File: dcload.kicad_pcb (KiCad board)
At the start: 2 copper layers, 251.4 x 94.7 mm, 12 parts

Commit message: General dimension tweaks
 - My understanding of exterior routing was incorrect resulting in
   unusable exterior dimensions.
 - Reduced tolerancing on D punches for tighter fit
 - Dropped LCD down slightly so not as close to edge
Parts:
- moved REF** 1.00 mm to (82.2, 48.8)
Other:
- board size 251.4 x 94.7 mm -> 249.8 x 93.1 mm
- board text added: "Exterior Dimensions: 249.81mm x 93.14mm"
- board text added: "July 7, 2018 V2 Phelps Williams"
- board text removed: "July 1, 2018 V1 Phelps Williams"
- board text removed: "Notes: - Exterior Routing with 1.6mm bit - Interior Nonplated Slots with 0.8mm bit - Exterior Dimensions: 249.81mm x 93.14mm"
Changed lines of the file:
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@@
     (links 0)
     (no_connects 0)
-    (area 13.099999 -113.850001 590.350001 126.71)
+    (area 15.024999 16.524999 264.985001 124.16)
     (thickness 1.6)
     (drawings 31)
@@
     (pad_to_mask_clearance 0.2)
     (aux_axis_origin 0 0)
-    (visible_elements FFFFFF7F)
+    (visible_elements FFFFFF6F)
     (pcbplotparams
       (layerselection 0x012f0_80000001)
@@
       (psa4output false)
       (plotreference true)
-      (plotvalue true)
+      (plotvalue false)
       (plotinvisibletext false)
       (padsonsilk false)
@@
       (drillshape 0)
       (scaleselection 1)
-      (outputdirectory ""))
+      (outputdirectory gerbers/))
   )
   (net 0 "")
@@
     (uvia_drill 0.1)
   )
-  (module p_panel_holes:Keystone_4093_DualBindingPost (layer F.Cu)
-    (at 120 94.25)
-    (fp_text reference REF** (at 0 -7.35) (layer F.SilkS) hide
-      (effects (font (size 1 1) (thickness 0.15)))
-    )
-    (fp_text value Keystone_4093_DualBindingPost (at 0 7.8) (layer F.Fab) hide
-      (effects (font (size 1 1) (thickness 0.15)))
-    )
-    (fp_line (start -15.225 -3.1) (end -15.225 3.1) (layer Edge.Cuts) (width 0.8))
-    (fp_arc (start -9.525 0) (end -15.225 -3.1) (angle 301.5) (layer Edge.Cuts) (width 0.8))
-    (fp_arc (start 9.525 0) (end 3.825 -3.1) (angle 301.5) (layer Edge.Cuts) (width 0.8))
-    (fp_line (start 3.825 -3.1) (end 3.825 3.1) (layer Edge.Cuts) (width 0.8))
-  )
   (module p_panel_holes:100DP1T1B1M1QEH (layer F.Cu)
     (at 90 94.25 180)
@@
   )
   (module p_panel_holes:LCD_Panel (layer F.Cu)
-    (at 82.25 47.75)
+    (at 82.25 48.75)
     (fp_text reference REF** (at 0 0.5) (layer F.SilkS)
       (effects (font (size 1 1) (thickness 0.15)))
@@
     (fp_line (start 49.1 30) (end -49.1 30) (layer B.SilkS) (width 0.15))
     (fp_line (start -49.1 30) (end -49.1 -30) (layer B.SilkS) (width 0.15))
-    (fp_line (start -48.9 -20.1) (end 48.9 -20.1) (layer Edge.Cuts) (width 0.8))
-    (fp_line (start 48.9 -20.1) (end 48.9 20.1) (layer Edge.Cuts) (width 0.8))
-    (fp_line (start 48.9 20.1) (end -48.9 20.1) (layer Edge.Cuts) (width 0.8))
-    (fp_line (start -48.9 20.1) (end -48.9 -20.1) (layer Edge.Cuts) (width 0.8))
+    (fp_line (start -48.9 -20.1) (end 48.9 -20.1) (layer Edge.Cuts) (width 0.15))
+    (fp_line (start 48.9 -20.1) (end 48.9 20.1) (layer Edge.Cuts) (width 0.15))
+    (fp_line (start 48.9 20.1) (end -48.9 20.1) (layer Edge.Cuts) (width 0.15))
+    (fp_line (start -48.9 20.1) (end -48.9 -20.1) (layer Edge.Cuts) (width 0.15))
     (pad "" np_thru_hole circle (at -46.5 27.5) (size 3.5 3.5) (drill 3.5) (layers *.Cu *.Mask))
     (pad "" np_thru_hole circle (at -46.5 -27.5) (size 3.5 3.5) (drill 3.5) (layers *.Cu *.Mask))
@@
       (effects (font (size 1 1) (thickness 0.15)))
     )
-    (fp_line (start -15.225 -3.1) (end -15.225 3.1) (layer Edge.Cuts) (width 0.8))
-    (fp_arc (start -9.525 0) (end -15.225 -3.1) (angle 301.5) (layer Edge.Cuts) (width 0.8))
-    (fp_arc (start 9.525 0) (end 3.825 -3.1) (angle 301.5) (layer Edge.Cuts) (width 0.8))
-    (fp_line (start 3.825 -3.1) (end 3.825 3.1) (layer Edge.Cuts) (width 0.8))
-  )
-  (module p_panel_holes:VB1094-75 (layer F.Cu)
-    (at 245.75 63)
-    (fp_text reference REF** (at 0 6.05) (layer F.SilkS) hide
-      (effects (font (size 1 1) (thickness 0.15)))
-    )
-    (fp_text value VB1094-75 (at 0.05 -5.85) (layer F.Fab) hide
-      (effects (font (size 1 1) (thickness 0.15)))
-    )
-    (fp_arc (start 0 0) (end -4.25 -2.67) (angle 295.5) (layer Edge.Cuts) (width 0.8))
-    (fp_line (start -4.25 -2.65) (end -4.25 2.65) (layer Edge.Cuts) (width 0.8))
-    (fp_circle (center 0 0) (end 1.5 0) (layer B.SilkS) (width 0.15))
+    (fp_line (start -15.065 -3.11) (end -15.065 3.11) (layer Edge.Cuts) (width 0.15))
+    (fp_arc (start -9.525 0) (end -15.065 -3.11) (angle 301.3) (layer Edge.Cuts) (width 0.15))
+    (fp_arc (start 9.525 0) (end 3.985 -3.11) (angle 301.3) (layer Edge.Cuts) (width 0.15))
+    (fp_line (start 3.985 -3.11) (end 3.985 3.11) (layer Edge.Cuts) (width 0.15))
+  )
+  (module p_panel_holes:Keystone_4093_DualBindingPost (layer F.Cu)
+    (at 120 94.25)
+    (fp_text reference REF** (at 0 -7.35) (layer F.SilkS) hide
+      (effects (font (size 1 1) (thickness 0.15)))
+    )
+    (fp_text value Keystone_4093_DualBindingPost (at 0 7.8) (layer F.Fab) hide
+      (effects (font (size 1 1) (thickness 0.15)))
+    )
+    (fp_line (start -15.065 -3.11) (end -15.065 3.11) (layer Edge.Cuts) (width 0.15))
+    (fp_arc (start -9.525 0) (end -15.065 -3.11) (angle 301.3) (layer Edge.Cuts) (width 0.15))
+    (fp_arc (start 9.525 0) (end 3.985 -3.11) (angle 301.3) (layer Edge.Cuts) (width 0.15))
+    (fp_line (start 3.985 -3.11) (end 3.985 3.11) (layer Edge.Cuts) (width 0.15))
   )
   (module p_panel_holes:5x4_Matrix_Keypad (layer F.Cu)
@@
     (fp_line (start -1 36.5) (end 1 36.5) (layer F.SilkS) (width 0.15))
     (fp_line (start -42.55 -1) (end -42.55 1) (layer F.SilkS) (width 0.15))
-    (fp_line (start -39.55 -35) (end -13.05 -35) (layer Edge.Cuts) (width 0.8))
-    (fp_line (start -13.05 -35) (end -13.05 -31.5) (layer Edge.Cuts) (width 0.8))
-    (fp_line (start -13.05 -31.5) (end -39.55 -31.5) (layer Edge.Cuts) (width 0.8))
-    (fp_line (start -39.55 -31.5) (end -39.55 -35) (layer Edge.Cuts) (width 0.8))
+    (fp_line (start -39.05 -35) (end -13.55 -35) (layer Edge.Cuts) (width 0.15))
+    (fp_line (start -13.55 -35) (end -13.55 -31.5) (layer Edge.Cuts) (width 0.15))
+    (fp_line (start -13.55 -31.5) (end -39.05 -31.5) (layer Edge.Cuts) (width 0.15))
+    (fp_line (start -39.05 -31.5) (end -39.05 -35) (layer Edge.Cuts) (width 0.15))
     (fp_line (start -42.55 36.5) (end -42.55 -36.5) (layer B.SilkS) (width 0.15))
     (fp_line (start -42.55 -36.5) (end 42.55 -36.5) (layer B.SilkS) (width 0.15))
@@
     (fp_line (start 42.55 36.5) (end -42.55 36.5) (layer B.SilkS) (width 0.15))
   )
-  (gr_text "July 1, 2018\nV1\nPhelps Williams" (at 191.75 57) (layer B.SilkS)
+  (module p_panel_holes:VB1094-75 (layer F.Cu)
+    (at 245.75 63)
+    (fp_text reference REF** (at 0 6.05) (layer F.SilkS) hide
+      (effects (font (size 1 1) (thickness 0.15)))
+    )
+    (fp_text value VB1094-75 (at 0.05 -6.05) (layer F.Fab) hide
+      (effects (font (size 1 1) (thickness 0.15)))
+    )
+    (fp_arc (start 0 0) (end -4.05 -2.67) (angle 293) (layer Edge.Cuts) (width 0.15))
+    (fp_line (start -4.05 -2.67) (end -4.05 2.67) (layer Edge.Cuts) (width 0.15))
+    (fp_circle (center 0 0) (end 1.5 0) (layer B.SilkS) (width 0.15))
+  )
+  (gr_text "July 7, 2018\nV2\nPhelps Williams" (at 191.75 57) (layer B.SilkS)
     (effects (font (size 1.5 1.5) (thickness 0.3)) (justify left mirror))
   )
@@
     (effects (font (size 2 2) (thickness 0.45)))
   )
-  (gr_text "DC Electronic Load" (at 82.25 22.5) (layer F.SilkS)
+  (gr_text "DC Electronic Load" (at 82.25 23) (layer F.SilkS)
     (effects (font (size 3 3) (thickness 0.6)))
   )
@@
   (gr_line (start 255.255 44.08) (end 255.255 82.26) (angle 90) (layer Eco1.User) (width 0.15))
   (gr_line (start 24.755 82.26) (end 24.755 44.08) (angle 90) (layer Eco1.User) (width 0.15))
-  (gr_arc (start 259.37 22.14) (end 259.37 15.8) (angle 90) (layer Edge.Cuts) (width 1.6))
-  (gr_arc (start 259.37 104.2) (end 265.71 104.2) (angle 90) (layer Edge.Cuts) (width 1.6))
-  (gr_arc (start 20.64 104.2) (end 20.64 110.54) (angle 90) (layer Edge.Cuts) (width 1.6))
-  (gr_text "Notes:\n - Exterior Routing with 1.6mm bit\n - Interior Nonplated Slots with 0.8mm bit\n - Exterior Dimensions: 249.81mm x 93.14mm" (at 119.14 122.81) (layer Cmts.User)
+  (gr_arc (start 259.37 22.14) (end 259.37 16.6) (angle 90) (layer Edge.Cuts) (width 0.15))
+  (gr_arc (start 259.37 104.2) (end 264.91 104.2) (angle 90) (layer Edge.Cuts) (width 0.15))
+  (gr_arc (start 20.64 104.2) (end 20.64 109.74) (angle 90) (layer Edge.Cuts) (width 0.15))
+  (gr_text "Exterior Dimensions: 249.81mm x 93.14mm" (at 119.14 122.81) (layer Cmts.User)
     (effects (font (size 1.5 1.5) (thickness 0.3)) (justify left))
   )
-  (gr_arc (start 20.64 22.14) (end 14.3 22.14) (angle 90) (layer Edge.Cuts) (width 1.6))
-  (gr_line (start 14.3 104.2) (end 14.3 22.14) (angle 90) (layer Edge.Cuts) (width 1.6))
-  (gr_line (start 259.37 110.54) (end 20.64 110.54) (angle 90) (layer Edge.Cuts) (width 1.6))
-  (gr_line (start 265.71 22.14) (end 265.71 104.2) (angle 90) (layer Edge.Cuts) (width 1.6))
-  (gr_line (start 20.64 15.8) (end 259.37 15.8) (angle 90) (layer Edge.Cuts) (width 1.6))
+  (gr_arc (start 20.64 22.14) (end 15.1 22.14) (angle 90) (layer Edge.Cuts) (width 0.15))
+  (gr_line (start 15.1 104.2) (end 15.1 22.14) (angle 90) (layer Edge.Cuts) (width 0.15))
+  (gr_line (start 259.37 109.74) (end 20.64 109.74) (angle 90) (layer Edge.Cuts) (width 0.15))
+  (gr_line (start 264.91 22.14) (end 264.91 104.2) (angle 90) (layer Edge.Cuts) (width 0.15))
+  (gr_line (start 20.64 16.6) (end 259.37 16.6) (angle 90) (layer Edge.Cuts) (width 0.15))
   (gr_line (start 15.1 109.74) (end 15.1 16.6) (angle 90) (layer Eco1.User) (width 0.15))
   (gr_line (start 264.91 109.74) (end 15.1 109.74) (angle 90) (layer Eco1.User) (width 0.15))

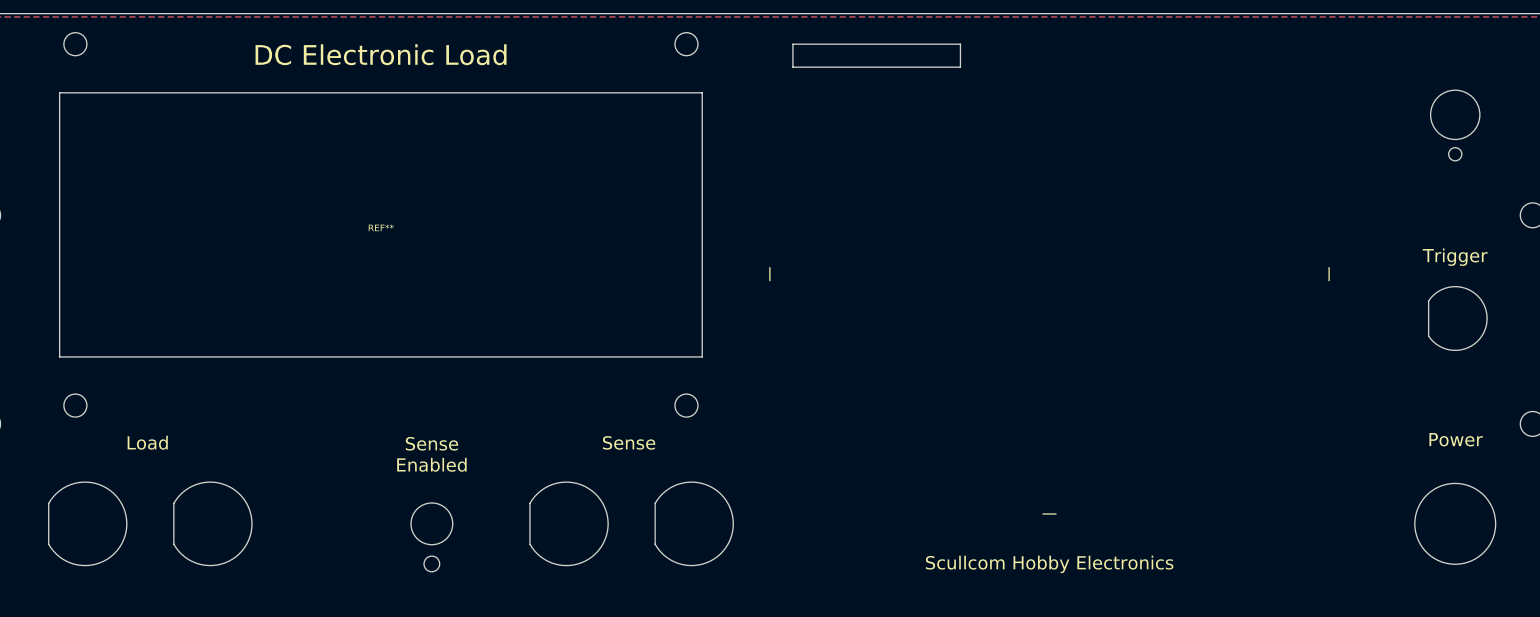
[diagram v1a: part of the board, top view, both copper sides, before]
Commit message: V3 with front panel USB port
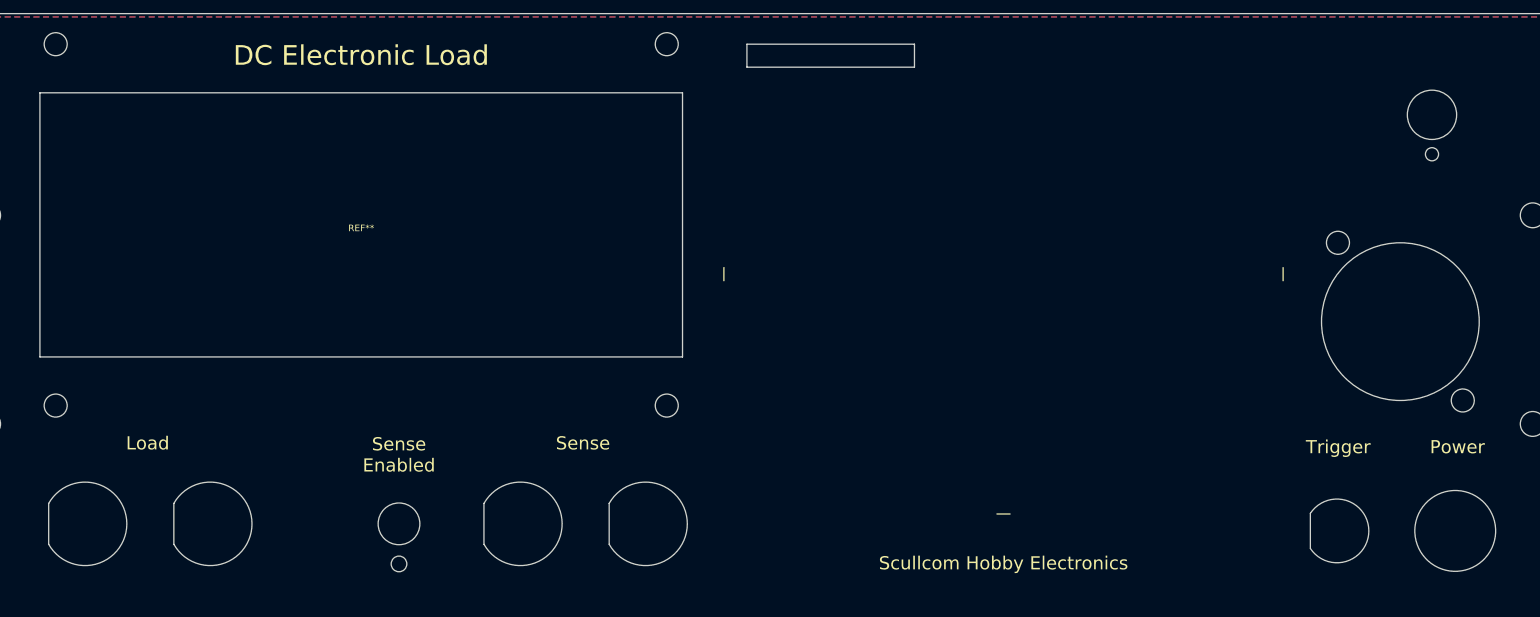
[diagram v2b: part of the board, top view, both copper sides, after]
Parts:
- added REF**: E3FRA, p_panel_holes:E3FRA, F.Cu at (237.4, 63.5)
- moved REF** 37.0 mm to (227.8, 95.3)
- moved REF** 7.00 mm to (113.0, 94.2)
- moved REF** 7.00 mm to (177.0, 56.2)
- moved REF** 5.00 mm to (85.0, 94.2)
- moved REF** 3.54 mm to (242.2, 32.0)
- moved REF** 3.00 mm to (79.2, 48.8)
- moved REF** 1.08 mm to (245.8, 95.3)
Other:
- board text added: "July 14, 2018 V3 Phelps Williams"
- board text removed: "July 7, 2018 V2 Phelps Williams"
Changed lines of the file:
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@@
     (tracks 0)
     (zones 0)
-    (modules 12)
+    (modules 13)
     (nets 1)
   )
@@
     (40 Dwgs.User user)
     (41 Cmts.User user)
-    (42 Eco1.User user hide)
+    (42 Eco1.User user)
     (43 Eco2.User user)
     (44 Edge.Cuts user)
@@
     (mod_text_size 1 1)
     (mod_text_width 0.15)
-    (pad_size 3.78 3.78)
-    (pad_drill 3.78)
+    (pad_size 24 24)
+    (pad_drill 24)
     (pad_to_mask_clearance 0.2)
     (aux_axis_origin 0 0)
@@
   )
   (module p_panel_holes:100DP1T1B1M1QEH (layer F.Cu)
-    (at 90 94.25 180)
+    (at 85 94.25 180)
     (fp_text reference REF** (at -3.85 8 180) (layer F.SilkS) hide
       (effects (font (size 1 1) (thickness 0.15)))
@@
   )
   (module p_panel_holes:EN11-HSM1AF15 (layer F.Cu)
-    (at 245.75 32)
+    (at 242.2125 32)
     (fp_text reference REF** (at 0 7.75) (layer F.SilkS) hide
       (effects (font (size 1 1) (thickness 0.15)))
@@
   )
   (module p_panel_holes:NKK_Switch_KB-R (layer F.Cu)
-    (at 245.75 94.25)
+    (at 245.75 95.325)
     (fp_text reference REF** (at 0 10.25) (layer F.SilkS) hide
       (effects (font (size 1 1) (thickness 0.15)))
@@
   )
   (module p_panel_holes:LCD_Panel (layer F.Cu)
-    (at 82.25 48.75)
+    (at 79.25 48.75)
     (fp_text reference REF** (at 0 0.5) (layer F.SilkS)
       (effects (font (size 1 1) (thickness 0.15)))
@@
   )
   (module p_panel_holes:Keystone_4093_DualBindingPost (layer F.Cu)
-    (at 120 94.25)
+    (at 113 94.25)
     (fp_text reference REF** (at 0 -7.35) (layer F.SilkS) hide
       (effects (font (size 1 1) (thickness 0.15)))
@@
   )
   (module p_panel_holes:5x4_Matrix_Keypad (layer F.Cu)
-    (at 184 56.25)
+    (at 177 56.25)
     (fp_text reference REF** (at 0 0.5) (layer F.SilkS) hide
       (effects (font (size 1 1) (thickness 0.15)))
@@
   )
   (module p_panel_holes:VB1094-75 (layer F.Cu)
-    (at 245.75 63)
+    (at 227.75 95.325)
     (fp_text reference REF** (at 0 6.05) (layer F.SilkS) hide
       (effects (font (size 1 1) (thickness 0.15)))
@@
     (fp_circle (center 0 0) (end 1.5 0) (layer B.SilkS) (width 0.15))
   )
-  (gr_text "July 7, 2018\nV2\nPhelps Williams" (at 191.75 57) (layer B.SilkS)
-    (effects (font (size 1.5 1.5) (thickness 0.3)) (justify left mirror))
-  )
-  (gr_text "Scullcom Hobby Electronics" (at 184 100.25) (layer F.SilkS)
-    (effects (font (size 2 2) (thickness 0.45)))
-  )
-  (gr_text "DC Electronic Load" (at 82.25 23) (layer F.SilkS)
+  (module p_panel_holes:E3FRA (layer F.Cu)
+    (at 237.4 63.475)
+    (fp_text reference REF** (at -11 -16.5) (layer F.SilkS) hide
+      (effects (font (size 1 1) (thickness 0.15)))
+    )
+    (fp_text value E3FRA (at -10.75 16.5) (layer F.Fab) hide
+      (effects (font (size 1 1) (thickness 0.15)))
+    )
+    (fp_line (start 11.75 12.5) (end 13 12.5) (layer B.SilkS) (width 0.15))
+    (fp_line (start -13 12.5) (end 7 12.5) (layer B.SilkS) (width 0.15))
+    (fp_line (start -13 -15.5) (end 13 -15.5) (layer B.SilkS) (width 0.15))
+    (fp_line (start 13 -15.5) (end 13 15.5) (layer B.SilkS) (width 0.15))
+    (fp_line (start 13 15.5) (end -13 15.5) (layer B.SilkS) (width 0.15))
+    (fp_line (start -13 15.5) (end -13 -15.5) (layer B.SilkS) (width 0.15))
+    (pad "" np_thru_hole circle (at 0 0) (size 24 24) (drill 24) (layers *.Cu *.Mask F.SilkS))
+    (pad "" np_thru_hole circle (at -9.5 -12) (size 3.5 3.5) (drill 3.5) (layers *.Cu *.Mask F.SilkS))
+    (pad "" np_thru_hole circle (at 9.5 12) (size 3.5 3.5) (drill 3.5) (layers *.Cu *.Mask F.SilkS))
+  )
+  (gr_text "July 14, 2018\nV3\nPhelps Williams" (at 177 57) (layer B.SilkS)
+    (effects (font (size 1.5 1.5) (thickness 0.3)) (justify mirror))
+  )
+  (gr_text "Scullcom Hobby Electronics" (at 177 100.25) (layer F.SilkS)
+    (effects (font (size 2 2) (thickness 0.45)))
+  )
+  (gr_text "DC Electronic Load" (at 79.25 23) (layer F.SilkS)
     (effects (font (size 3 3) (thickness 0.6)))
   )
-  (gr_text "Sense\nEnabled" (at 90 83.75) (layer F.SilkS)
+  (gr_text "Sense\nEnabled" (at 85 83.75) (layer F.SilkS)
     (effects (font (size 2 2) (thickness 0.45)))
   )
@@
     (effects (font (size 2 2) (thickness 0.45)))
   )
-  (gr_text Sense (at 120 82) (layer F.SilkS)
-    (effects (font (size 2 2) (thickness 0.45)))
-  )
-  (gr_text Trigger (at 245.75 53.5) (layer F.SilkS)
-    (effects (font (size 2 2) (thickness 0.45)))
-  )
-  (gr_text Power (at 245.75 81.5) (layer F.SilkS)
-    (effects (font (size 2 2) (thickness 0.45)))
-  )
-  (gr_line (start 79.705 79.7) (end 79.705 109.7) (angle 90) (layer Dwgs.User) (width 0.15))
-  (gr_line (start 72.505 79.7) (end 72.505 109.7) (angle 90) (layer Dwgs.User) (width 0.15))
-  (gr_line (start 200.305 79.8) (end 200.305 109.7) (angle 90) (layer Dwgs.User) (width 0.15))
-  (gr_line (start 207.505 79.8) (end 207.505 109.7) (angle 90) (layer Dwgs.User) (width 0.15))
-  (gr_text "Keypad Connector" (at 158.125 77.35) (layer Dwgs.User)
+  (gr_text Sense (at 113 82) (layer F.SilkS)
+    (effects (font (size 2 2) (thickness 0.45)))
+  )
+  (gr_text Trigger (at 227.95 82.575) (layer F.SilkS)
+    (effects (font (size 2 2) (thickness 0.45)))
+  )
+  (gr_text Power (at 246.075 82.575) (layer F.SilkS)
+    (effects (font (size 2 2) (thickness 0.45)))
+  )
+  (gr_line (start 75.705 79.7) (end 75.705 109.7) (angle 90) (layer Dwgs.User) (width 0.15))
+  (gr_line (start 68.505 79.7) (end 68.505 109.7) (angle 90) (layer Dwgs.User) (width 0.15))
+  (gr_line (start 196.305 79.8) (end 196.305 109.7) (angle 90) (layer Dwgs.User) (width 0.15))
+  (gr_line (start 203.505 79.8) (end 203.505 109.7) (angle 90) (layer Dwgs.User) (width 0.15))
+  (gr_text "Keypad Connector" (at 154.125 77.35) (layer Dwgs.User)
     (effects (font (size 1.5 1.5) (thickness 0.3)))
   )
-  (gr_line (start 145.505 75) (end 170.005 75) (angle 90) (layer Dwgs.User) (width 0.15))
-  (gr_line (start 71.505 79.7) (end 208.505 79.7) (angle 90) (layer Dwgs.User) (width 0.2))
-  (gr_circle (center 245.75 32) (end 245.75 38.35) (layer Eco1.User) (width 0.15))
+  (gr_line (start 141.505 75) (end 166.005 75) (angle 90) (layer Dwgs.User) (width 0.15))
+  (gr_line (start 67.505 79.7) (end 204.505 79.7) (angle 90) (layer Dwgs.User) (width 0.2))
+  (gr_circle (center 242.2125 32) (end 242.2125 38.35) (layer Eco1.User) (width 0.15))
   (gr_line (start 255.255 44.08) (end 255.255 82.26) (angle 90) (layer Eco1.User) (width 0.15))
   (gr_line (start 24.755 82.26) (end 24.755 44.08) (angle 90) (layer Eco1.User) (width 0.15))
